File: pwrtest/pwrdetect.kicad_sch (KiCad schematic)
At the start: 42 parts, among them Q1 BC857, Q2 BC857, Q3 BC857, Q7 BC847, Q8 BC847, U11 TL431, U12 TL431, U6 TL431DBZ, U7 TL431DBZ, U8 TL431DBZ

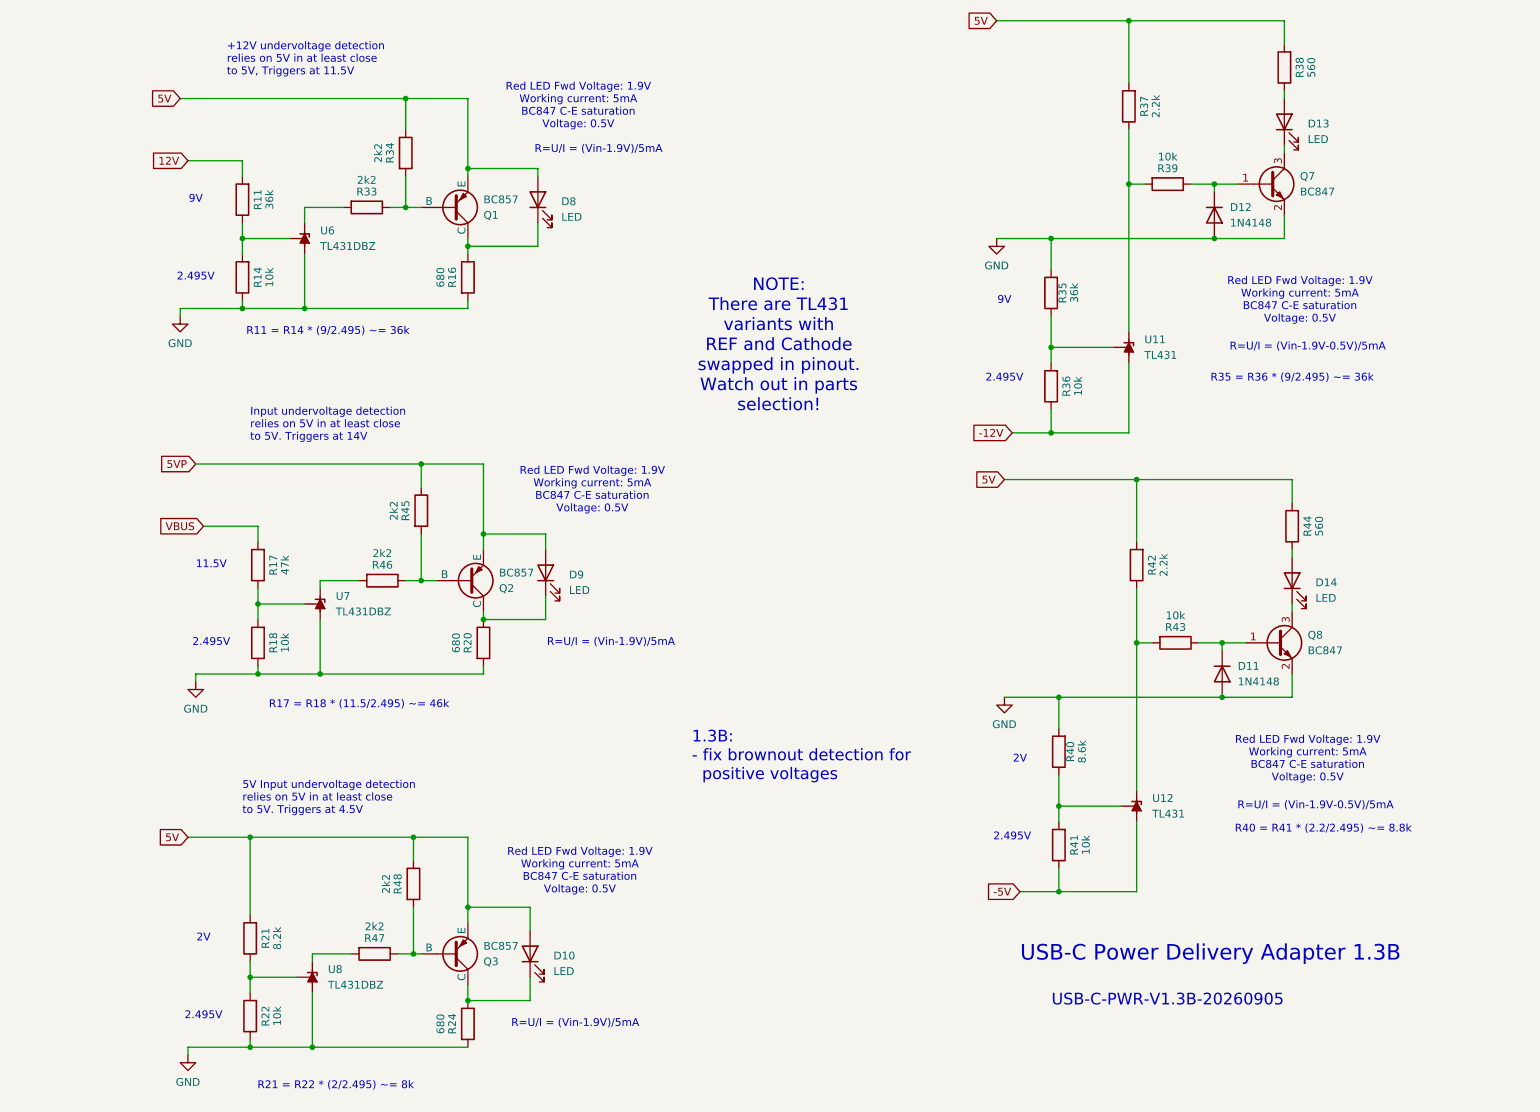
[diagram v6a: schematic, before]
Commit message: add 3.3V and 9V to usb pwr
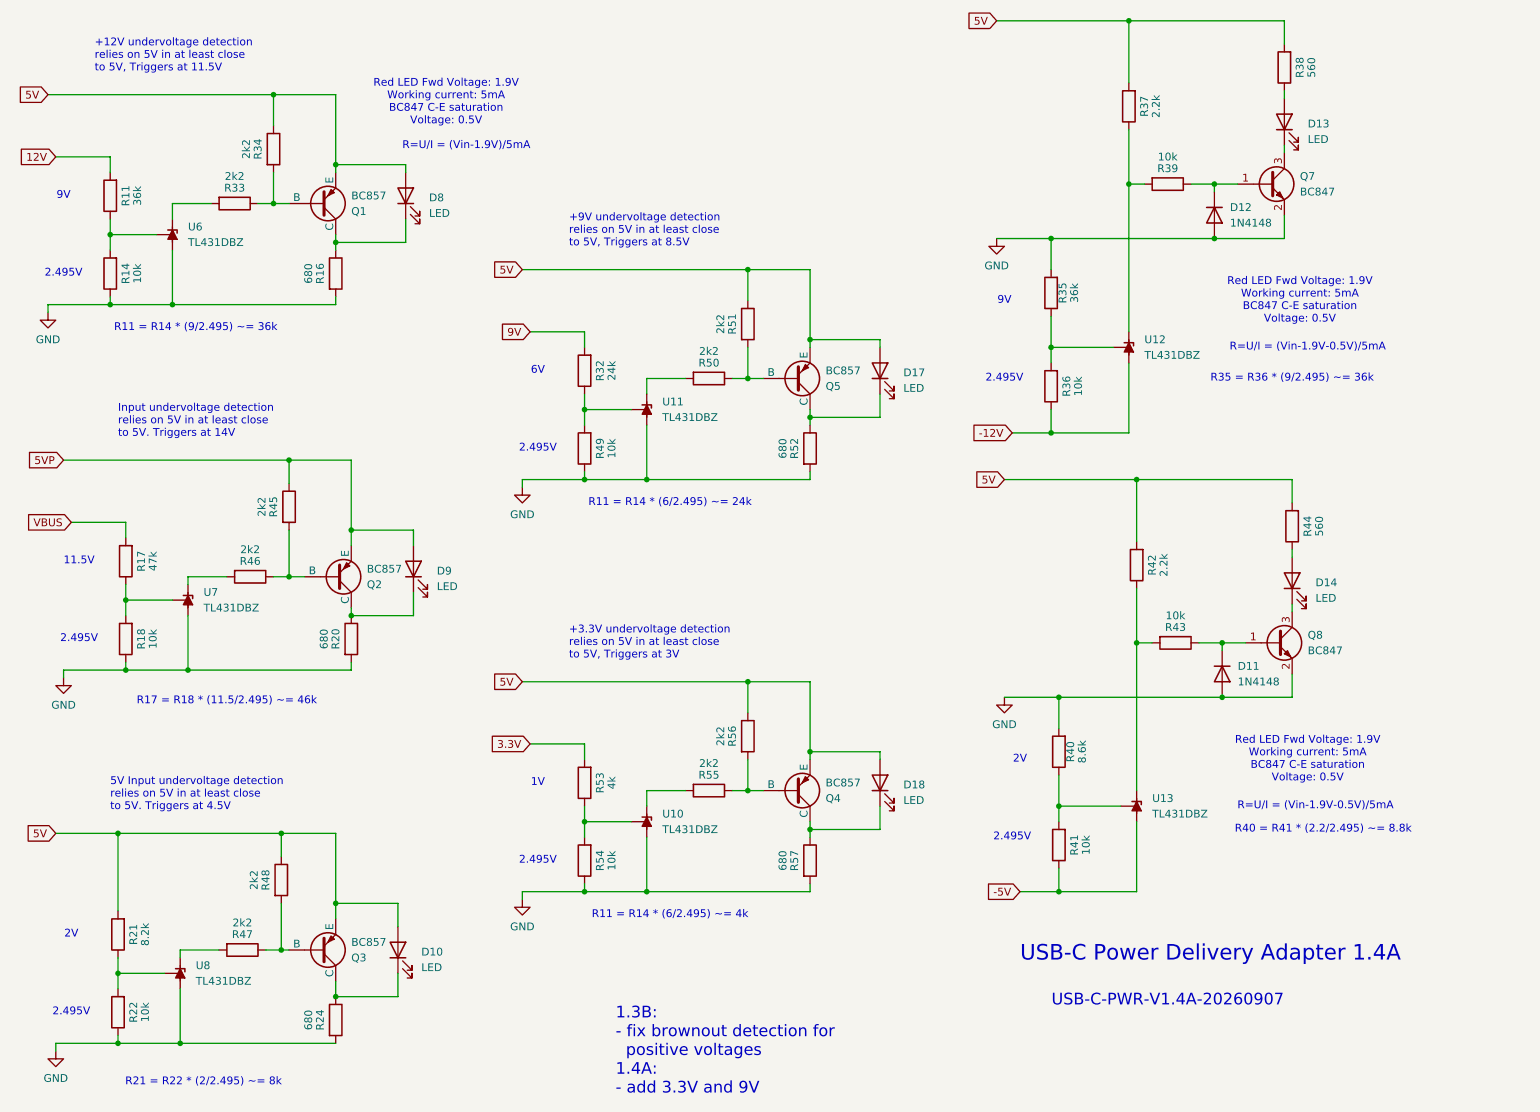
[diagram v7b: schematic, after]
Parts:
- added D17, D18: LED, Diode_SMD:D_0603_1608Metric_Pad1.05x0.95mm_HandSolder, symbol Device:LED
- added Q4, Q5: BC857, Package_TO_SOT_SMD:SOT-23, symbol Simulation_SPICE:PNP
- added R32: 24k, Resistor_SMD:R_0603_1608Metric_Pad0.98x0.95mm_HandSolder, symbol Device:R
- added R49, R54: 10k, Resistor_SMD:R_0603_1608Metric_Pad0.98x0.95mm_HandSolder, symbol Device:R
- added R50, R51, R55, R56: 2k2, Resistor_SMD:R_0603_1608Metric_Pad0.98x0.95mm_HandSolder, symbol Device:R
- added R52, R57: 680, Resistor_SMD:R_0603_1608Metric_Pad0.98x0.95mm_HandSolder, symbol Device:R
- added R53: 4k, Resistor_SMD:R_0603_1608Metric_Pad0.98x0.95mm_HandSolder, symbol Device:R
- added U10, U13: TL431DBZ, Package_TO_SOT_SMD:SOT-23, symbol Reference_Voltage:TL431DBZ
- Q1, Q2, Q3: LCSC (none) -> C20069137
- U11, U12: value TL431 -> TL431DBZ; LCSC (none) -> C181103
- U6, U7, U8: LCSC (none) -> C181103
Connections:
- net -12V: now also U12.3 (A); no longer U11.3 (A)
- net -5V: now also U13.3 (A); no longer U12.3 (A)
- net 5V: now also Q1.2 (E), Q3.2 (E), D17.2 (A), D18.2 (A), Q4.2 (E), Q5.2 (E), R51.1, R56.1; no longer Q1.3 (E), Q3.3 (E)
- net 5VP: now also Q2.2 (E); no longer Q2.3 (E)
- net GND: now also U11.3 (A), R49.1, R52.2, R54.1, R57.2, U10.3 (A)
- net at R42.1, R43.2: now also U13.2 (K); no longer U12.1 (K)
- net at D9.1 (K), R20.1: now also Q2.3 (C); no longer Q2.1 (C)
- net at R45.2, R46.1: now also Q2.1 (B); no longer Q2.2 (B)
- net at D8.1 (K), R16.1: now also Q1.3 (C); no longer Q1.1 (C)
- net at R47.1, R48.2: now also Q3.1 (B); no longer Q3.2 (B)
- net at R40.1, R41.2: now also U13.1 (REF); no longer U12.2 (REF)
- net at R21.1, R22.2: now also U8.1 (REF); no longer U8.2 (REF)
- net at R33.1, R34.2: now also Q1.1 (B); no longer Q1.2 (B)
- net at R33.2: now also U6.2 (K); no longer U6.1 (K)
- net at D10.1 (K), R24.1: now also Q3.3 (C); no longer Q3.1 (C)
- net at R11.1, R14.2: now also U6.1 (REF); no longer U6.2 (REF)
- net at R47.2: now also U8.2 (K); no longer U8.1 (K)
- net at R37.1, R39.2: now also U12.2 (K); no longer U11.1 (K)
- net at R35.1, R36.2: now also U12.1 (REF); no longer U11.2 (REF)
- net at R17.1, R18.2: now also U7.1 (REF); no longer U7.2 (REF)
- net at R46.2: now also U7.2 (K); no longer U7.1 (K)
- new net: D17.1 (K), Q5.3 (C), R52.1
- new net: D18.1 (K), Q4.3 (C), R57.1
- new net: R53.1, R54.2, U10.1 (REF)
- new net: Q4.1 (B), R55.1, R56.2
- new net: R55.2, U10.2 (K)
- new net: R32.1, R49.2, U11.1 (REF)
- new net: Q5.1 (B), R50.1, R51.2
- new net: R50.2, U11.2 (K)
- new net 3.3V: R53.2
- new net 9V: R32.2
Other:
- note added: "+3.3V undervoltage detection relies on 5V in at least close to 5V, Triggers at 3V"
- note added: "+9V undervoltage detection relies on 5V in at least close to 5V, Triggers at 8.5V"
- note added: "1.3B: - fix brownout detection for positive voltages 1.4A: - add 3.3V and 9V"
- note added: "1V"
- note added: "6V"
- note added: "R11 = R14 * (6/2.495) ~= 24k"
- note added: "R11 = R14 * (6/2.495) ~= 4k"
- note added: "USB-C Power Delivery Adapter 1.4A"
- note added: "USB-C-PWR-V1.4A-20260907"
- note removed: "1.3B: - fix brownout detection for positive voltages"
- note removed: "NOTE: There are TL431 variants with REF and Cathode swapped in pinout. Watch out in parts selection!"
- note removed: "USB-C Power Delivery Adapter 1.3B"
- note removed: "USB-C-PWR-V1.3B-20260905"
- moved on the sheet: D10, D8, D9, Q1, R11, R14, R16, R17, R18, R20, R21, R22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

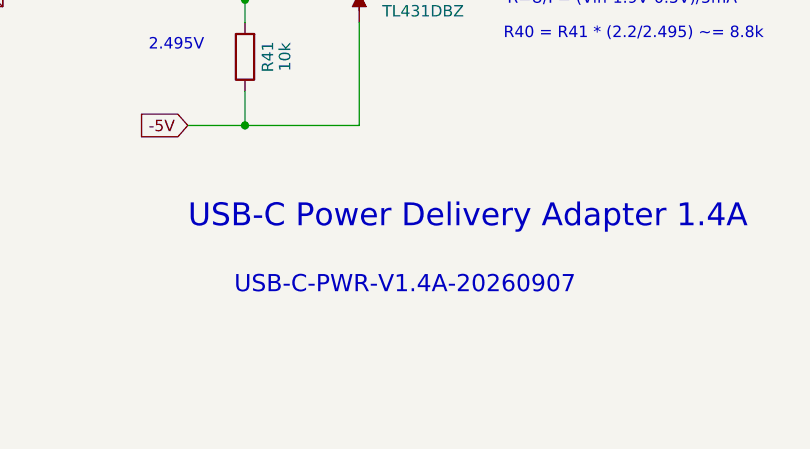
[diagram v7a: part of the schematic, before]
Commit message: update usb-c pwr adapter with mounting holes
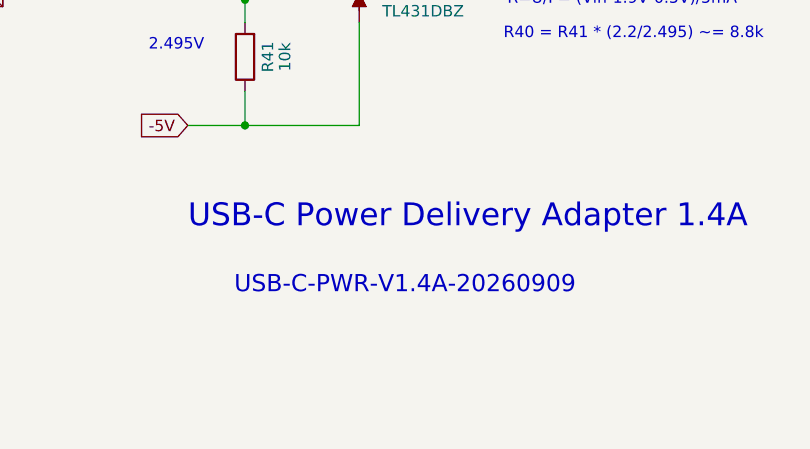
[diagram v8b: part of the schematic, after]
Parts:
- D10, D13, D14, D17, D18, D8, D9: footprint Diode_SMD:D_0603_1608Metric_Pad1.05x0.95mm_HandSolder -> Diode_SMD:D_0805_2012Metric_Pad1.15x1.40mm_HandSolder; LCSC C7496820 -> C84256
- R16, R20, R24, R52, R57: LCSC (none) -> C23228
- R32: LCSC (none) -> C23352
- R33, R34, R45, R46, R47, R48, R50, R51, R55, R56: LCSC (none) -> C4190
- R53: LCSC (none) -> C23018
- U6, U7, U8: LCSC C181103 -> C19272793
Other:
- note added: "USB-C-PWR-V1.4A-20260909"
- note removed: "USB-C-PWR-V1.4A-20260907"
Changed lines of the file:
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@@
 		)
 	)
-	(text "USB-C-PWR-V1.4A-20260907"
+	(text "USB-C-PWR-V1.4A-20260909"
 		(exclude_from_sim no)
 		(at 210.82 177.8 0)
@@
 			)
 		)
-		(property "LCSC" ""
+		(property "LCSC" "C23228"
 			(at 149.86 87.63 0)
 			(hide yes)
@@
 			)
 		)
-		(property "Footprint" "Diode_SMD:D_0603_1608Metric_Pad1.05x0.95mm_HandSolder"
+		(property "Footprint" "Diode_SMD:D_0805_2012Metric_Pad1.15x1.40mm_HandSolder"
 			(at 86.36 46.355 0)
 			(hide yes)
@@
 			)
 		)
-		(property "LCSC" "C7496820"
+		(property "LCSC" "C84256"
 			(at 90.17 46.6724 0)
 			(hide yes)
@@
 			)
 		)
-		(property "LCSC" "C181103"
+		(property "LCSC" "C19272793"
 			(at 49.53 173.355 0)
 			(hide yes)
@@
 			)
 		)
-		(property "LCSC" ""
+		(property "LCSC" "C4190"
 			(at 63.5 158.115 0)
 			(hide yes)
@@
 			)
 		)
-		(property "LCSC" ""
+		(property "LCSC" "C4190"
 			(at 58.42 45.085 0)
 			(hide yes)
@@
 			)
 		)
-		(property "Footprint" "Diode_SMD:D_0603_1608Metric_Pad1.05x0.95mm_HandSolder"
+		(property "Footprint" "Diode_SMD:D_0805_2012Metric_Pad1.15x1.40mm_HandSolder"
 			(at 231.14 109.22 0)
 			(hide yes)
@@
 			)
 		)
-		(property "LCSC" "C7496820"
+		(property "LCSC" "C84256"
 			(at 234.95 109.5374 0)
 			(hide yes)
@@
 			)
 		)
-		(property "Footprint" "Diode_SMD:D_0603_1608Metric_Pad1.05x0.95mm_HandSolder"
+		(property "Footprint" "Diode_SMD:D_0805_2012Metric_Pad1.15x1.40mm_HandSolder"
 			(at 85.09 169.545 0)
 			(hide yes)
@@
 			)
 		)
-		(property "LCSC" "C7496820"
+		(property "LCSC" "C84256"
 			(at 88.9 169.8624 0)
 			(hide yes)
@@
 			)
 		)
-		(property "LCSC" "C181103"
+		(property "LCSC" "C19272793"
 			(at 48.26 52.705 0)
 			(hide yes)
@@
 			)
 		)
-		(property "LCSC" "C181103"
+		(property "LCSC" "C19272793"
 			(at 50.8 112.395 0)
 			(hide yes)
@@
 			)
 		)
-		(property "Footprint" "Diode_SMD:D_0603_1608Metric_Pad1.05x0.95mm_HandSolder"
+		(property "Footprint" "Diode_SMD:D_0805_2012Metric_Pad1.15x1.40mm_HandSolder"
 			(at 163.83 142.24 0)
 			(hide yes)
@@
 			)
 		)
-		(property "LCSC" "C7496820"
+		(property "LCSC" "C84256"
 			(at 167.64 142.5574 0)
 			(hide yes)
@@
 			)
 		)
-		(property "LCSC" ""
+		(property "LCSC" "C4190"
 			(at 62.23 38.735 0)
 			(hide yes)
@@
 			)
 		)
-		(property "LCSC" ""
+		(property "LCSC" "C4190"
 			(at 135.89 140.97 0)
 			(hide yes)
@@
 			)
 		)
-		(property "Footprint" "Diode_SMD:D_0603_1608Metric_Pad1.05x0.95mm_HandSolder"
+		(property "Footprint" "Diode_SMD:D_0805_2012Metric_Pad1.15x1.40mm_HandSolder"
 			(at 229.87 34.29 0)
 			(hide yes)
@@
 			)
 		)
-		(property "LCSC" "C7496820"
+		(property "LCSC" "C84256"
 			(at 233.68 34.6074 0)
 			(hide yes)
@@
 			)
 		)
-		(property "LCSC" ""
+		(property "LCSC" "C4190"
 			(at 135.89 73.66 0)
 			(hide yes)
@@
 			)
 		)
-		(property "LCSC" ""
+		(property "LCSC" "C4190"
 			(at 139.7 67.31 0)
 			(hide yes)
@@
 			)
 		)
-		(property "LCSC" ""
+		(property "LCSC" "C23228"
 			(at 72.39 180.975 0)
 			(hide yes)
@@
 			)
 		)
-		(property "LCSC" ""
+		(property "LCSC" "C4190"
 			(at 139.7 134.62 0)
 			(hide yes)
@@
 			)
 		)
-		(property "LCSC" ""
+		(property "LCSC" "C23018"
 			(at 118.11 142.24 0)
 			(hide yes)
@@
 			)
 		)
-		(property "LCSC" ""
+		(property "LCSC" "C23228"
 			(at 149.86 154.94 0)
 			(hide yes)
@@
 			)
 		)
-		(property "LCSC" ""
+		(property "LCSC" "C4190"
 			(at 59.69 167.005 0)
 			(hide yes)
@@
 			)
 		)
-		(property "Footprint" "Diode_SMD:D_0603_1608Metric_Pad1.05x0.95mm_HandSolder"
+		(property "Footprint" "Diode_SMD:D_0805_2012Metric_Pad1.15x1.40mm_HandSolder"
 			(at 87.63 107.315 0)
 			(hide yes)
@@
 			)
 		)
-		(property "LCSC" "C7496820"
+		(property "LCSC" "C84256"
 			(at 91.44 107.6324 0)
 			(hide yes)
@@
 			)
 		)
-		(property "LCSC" ""
+		(property "LCSC" "C23352"
 			(at 118.11 74.93 0)
 			(hide yes)
@@
 			)
 		)
-		(property "LCSC" ""
+		(property "LCSC" "C23228"
 			(at 74.93 118.745 0)
 			(hide yes)
@@
 			)
 		)
-		(property "LCSC" ""
+		(property "LCSC" "C4190"
 			(at 64.77 97.155 0)
 			(hide yes)
@@
 			)
 		)
-		(property "Footprint" "Diode_SMD:D_0603_1608Metric_Pad1.05x0.95mm_HandSolder"
+		(property "Footprint" "Diode_SMD:D_0805_2012Metric_Pad1.15x1.40mm_HandSolder"
 			(at 163.83 74.93 0)
 			(hide yes)
@@
 			)
 		)
-		(property "LCSC" "C7496820"
+		(property "LCSC" "C84256"
 			(at 167.64 75.2474 0)
 			(hide yes)
@@
 			)
 		)
-		(property "LCSC" ""
+		(property "LCSC" "C23228"
 			(at 72.39 59.055 0)
 			(hide yes)
@@
 			)
 		)
-		(property "LCSC" ""
+		(property "LCSC" "C4190"
 			(at 60.96 106.045 0)
 			(hide yes)
